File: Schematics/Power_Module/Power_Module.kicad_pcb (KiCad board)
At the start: 4 copper layers, 69.5 x 60 mm, 1 part, among them J6 Stack Male Edge Connector

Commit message: Added PCB template
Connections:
- net Vbuck1 renamed 3.3V_A
- net Vbuck1.1 renamed 5.0V_A
- net Vbuck2 renamed 3.3V_B
- net Vin + renamed BATT_A
- net Vin - renamed GND
- net Vin 2+ renamed BATT_B
- net Vin2 - renamed GND2
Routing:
- added copper zone on In1.Cu, net GND
- added copper zone on In2.Cu, net GND
- removed copper zone on In1.Cu, net (none)
- removed copper zone on In2.Cu, net (none)
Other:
- board text added: "PLACE POWER CONNECTORS HERE (okay if on bottom)"
- board text removed: "Make sure connectors are at the front (on both sides is fine)"

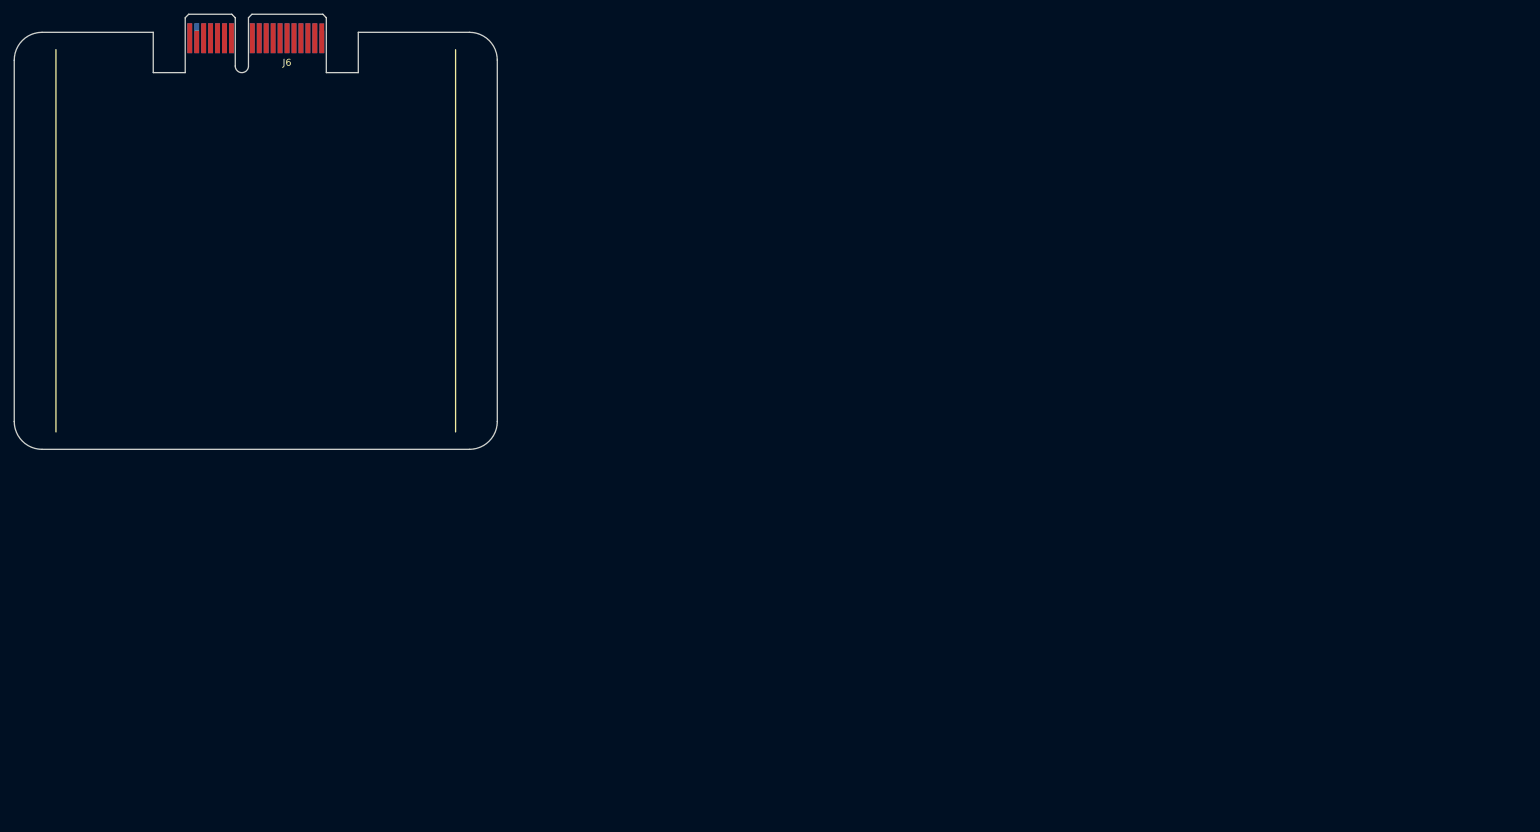
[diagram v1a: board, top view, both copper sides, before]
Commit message: Layout of 3.3V_A converter finished
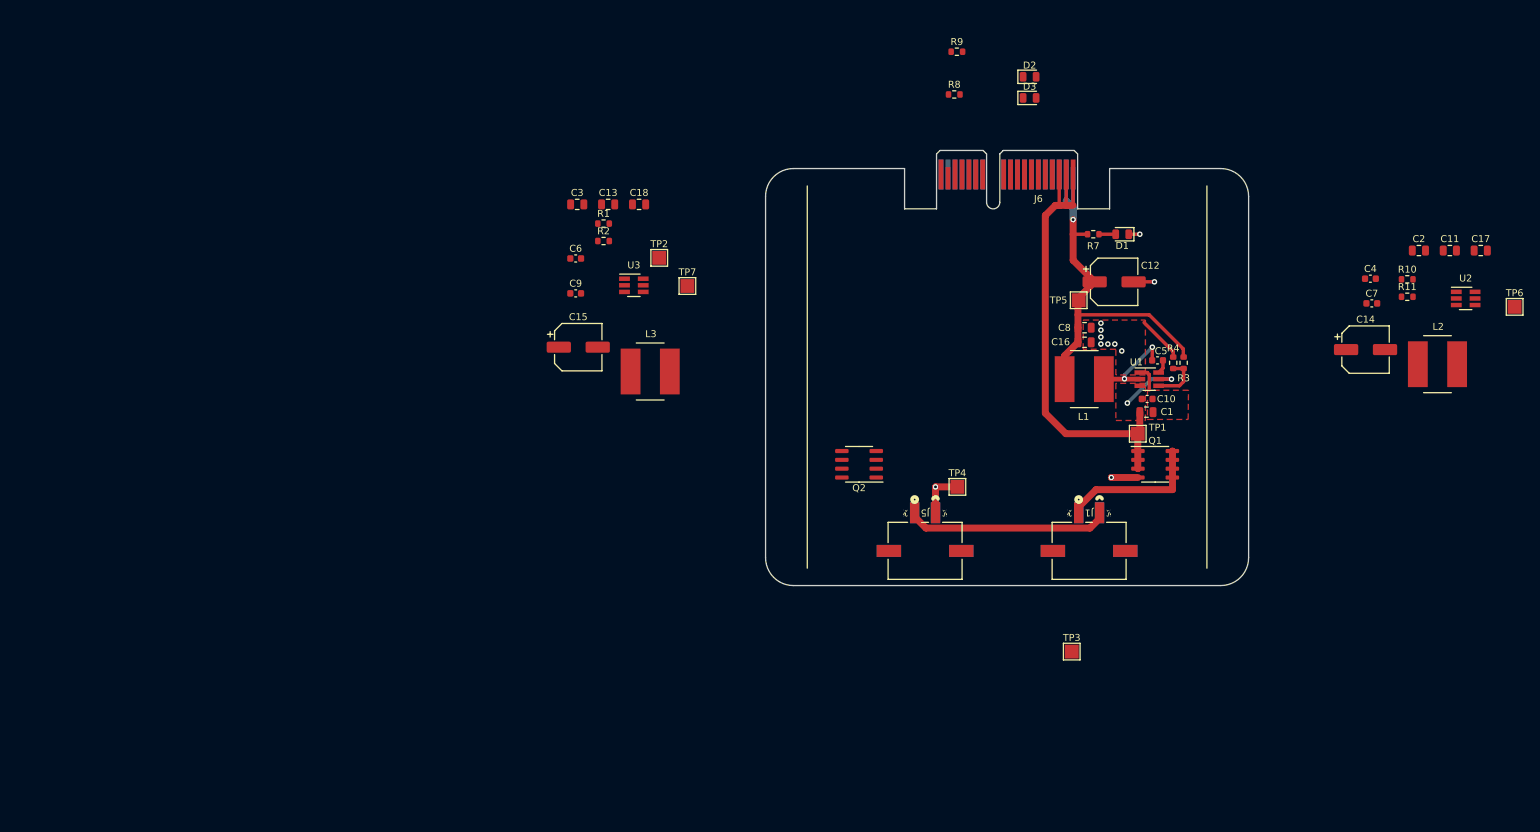
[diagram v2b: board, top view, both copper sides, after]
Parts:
- added C1: 4.7uF, Capacitor_SMD:C_0805_2012Metric, F.Cu at (185.1, 74.8)
- added C10: 100nF, Capacitor_SMD:C_0603_1608Metric, F.Cu at (185.2, 72.9)
- added C11: 22uF, Capacitor_SMD:C_0805_2012Metric, F.Cu at (228.7, 51.5)
- added C12: 100uF, Capacitor_SMD:CP_Elec_6.3x5.9, F.Cu at (180.4, 56.0)
- added C13: 22uF, Capacitor_SMD:C_0805_2012Metric, F.Cu at (107.6, 44.9)
- added C14: 100uF, Capacitor_SMD:CP_Elec_6.3x5.9, F.Cu at (216.6, 65.8)
- added C15: 100uF, Capacitor_SMD:CP_Elec_6.3x5.9, F.Cu at (103.3, 65.5)
- added C16: 22uF, Capacitor_SMD:C_0805_2012Metric, F.Cu at (176.2, 64.8)
- added C17: 22uF, Capacitor_SMD:C_0805_2012Metric, F.Cu at (233.2, 51.5)
- added C18: 22uF, Capacitor_SMD:C_0805_2012Metric, F.Cu at (112.0, 44.9)
- added C2: 4.7uF, Capacitor_SMD:C_0805_2012Metric, F.Cu at (224.2, 51.5)
- added C3: 4.7uF, Capacitor_SMD:C_0805_2012Metric, F.Cu at (103.2, 44.9)
- added C4: 100nF, Capacitor_SMD:C_0603_1608Metric, F.Cu at (217.3, 55.6)
- added C5: 100nF, Capacitor_SMD:C_0603_1608Metric, F.Cu at (186.7, 67.3)
- added C6: 100nF, Capacitor_SMD:C_0603_1608Metric, F.Cu at (102.9, 52.7)
- added C7: 100nF, Capacitor_SMD:C_0603_1608Metric, F.Cu at (217.5, 59.1)
- added C8: 22uF, Capacitor_SMD:C_0805_2012Metric, F.Cu at (176.2, 62.6)
- added C9: 100nF, Capacitor_SMD:C_0603_1608Metric, F.Cu at (102.9, 57.7)
- added D1: 3.3V_A PWR (GRN), LED_SMD:LED_0805_2012Metric, F.Cu at (181.6, 49.2)
- added D2: 5.0V_A PWR (RED), LED_SMD:LED_0805_2012Metric, F.Cu at (168.2, 26.6)
- added D3: 3.3V_B PWR (GRN), LED_SMD:LED_0805_2012Metric, F.Cu at (168.2, 29.6)
- added J1: ScrewSwitch A, footprints:CONN_2-1445057-2_TYCO, F.Cu at (178.3, 89.3)
- added J2: ScrewSwitch B, footprints:CONN_2-1445057-2_TYCO, B.Cu at (175.3, 89.3)
- added J3: Battery B, footprints:CONN_2-1445057-2_TYCO, B.Cu at (151.7, 89.3)
- added J5: Battery A, footprints:CONN_2-1445057-2_TYCO, F.Cu at (154.7, 89.3)
- added L1: 5.6uH, Inductor_SMD:L_Bourns_SRN8040TA, F.Cu at (176.1, 70.0)
- added L2: 6.8uH, Inductor_SMD:L_Bourns_SRN8040TA, F.Cu at (226.9, 67.9)
- added L3: 5.6uH, Inductor_SMD:L_Bourns_SRN8040TA, F.Cu at (113.7, 69.0)
- added Q1: AO4447A, Package_SO:SOIC-8_3.9x4.9mm_P1.27mm, F.Cu at (186.3, 82.3)
- added Q2: AO4447A, Package_SO:SOIC-8_3.9x4.9mm_P1.27mm, F.Cu at (143.7, 82.3)
- added R1: 100k, Resistor_SMD:R_0603_1608Metric, F.Cu at (106.9, 47.7)
- added R10: 56k, Resistor_SMD:R_0603_1608Metric, F.Cu at (222.6, 55.7)
- added R11: 7.5k, Resistor_SMD:R_0603_1608Metric, F.Cu at (222.6, 58.2)
- added R2: 22k, Resistor_SMD:R_0603_1608Metric, F.Cu at (106.9, 50.2)
- added R3: 100k, Resistor_SMD:R_0603_1608Metric, F.Cu at (190.4, 67.7)
- added R4: 22k, Resistor_SMD:R_0603_1608Metric, F.Cu at (188.9, 67.7)
- added R7: 510R, Resistor_SMD:R_0603_1608Metric, F.Cu at (177.4, 49.2)
- added R8: 2k, Resistor_SMD:R_0603_1608Metric, F.Cu at (157.4, 29.1)
- added R9: 510R, Resistor_SMD:R_0603_1608Metric, F.Cu at (157.8, 22.9)
- added TP1: TP_BATT1, TestPoint:TestPoint_Pad_2.0x2.0mm, F.Cu at (183.8, 77.9)
- added TP2: TP_BATT2, TestPoint:TestPoint_Pad_2.0x2.0mm, F.Cu at (115.0, 52.6)
- added TP3: TP_GND2, TestPoint:TestPoint_Pad_2.0x2.0mm, F.Cu at (174.3, 109.2)
- added TP4: TP_GND1, TestPoint:TestPoint_Pad_2.0x2.0mm, F.Cu at (157.8, 85.5)
- added TP5: TP_3.3V_A, TestPoint:TestPoint_Pad_2.0x2.0mm, F.Cu at (175.3, 58.7)
- added TP6: TP_5.0V_A, TestPoint:TestPoint_Pad_2.0x2.0mm, F.Cu at (238.0, 59.6)
- added TP7: TP_3.3V_B, TestPoint:TestPoint_Pad_2.0x2.0mm, F.Cu at (119.0, 56.6)
- added U1: LMR51430XDDCR, Package_TO_SOT_SMD:SOT-23-6_Handsoldering, F.Cu at (185.4, 70.0)
- added U2: LMR51430XDDCR, Package_TO_SOT_SMD:SOT-23-6_Handsoldering, F.Cu at (231.0, 58.4)
- added U3: LMR51430XDDCR, Package_TO_SOT_SMD:SOT-23-6_Handsoldering, F.Cu at (111.3, 56.5)
- moved J6 109.9 mm to (174.5, 40.6)
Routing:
- net BATT_A: track 0.00 -> 78.9 mm, vias 0 -> 2
- net 3.3V_A: track 0.00 -> 57.6 mm, vias 0 -> 1
- net Net-(J1-Pad1): track 0.00 -> 29.2 mm
- net GND: track 0.00 -> 25.7 mm, vias 0 -> 11
- net Net-(J1-Pad2): track 0.00 -> 20.9 mm
- net Net-(U1-SW): track 0.00 -> 13.3 mm, vias 0 -> 2
- net Net-(U1-FB): track 0.00 -> 7.22 mm
- net Net-(D1-A): track 0.00 -> 2.40 mm
- net Net-(U1-CB): track 0.00 -> 2.01 mm
- added copper zone on F.Cu, net BATT_A
- added copper zone on F.Cu, net GND

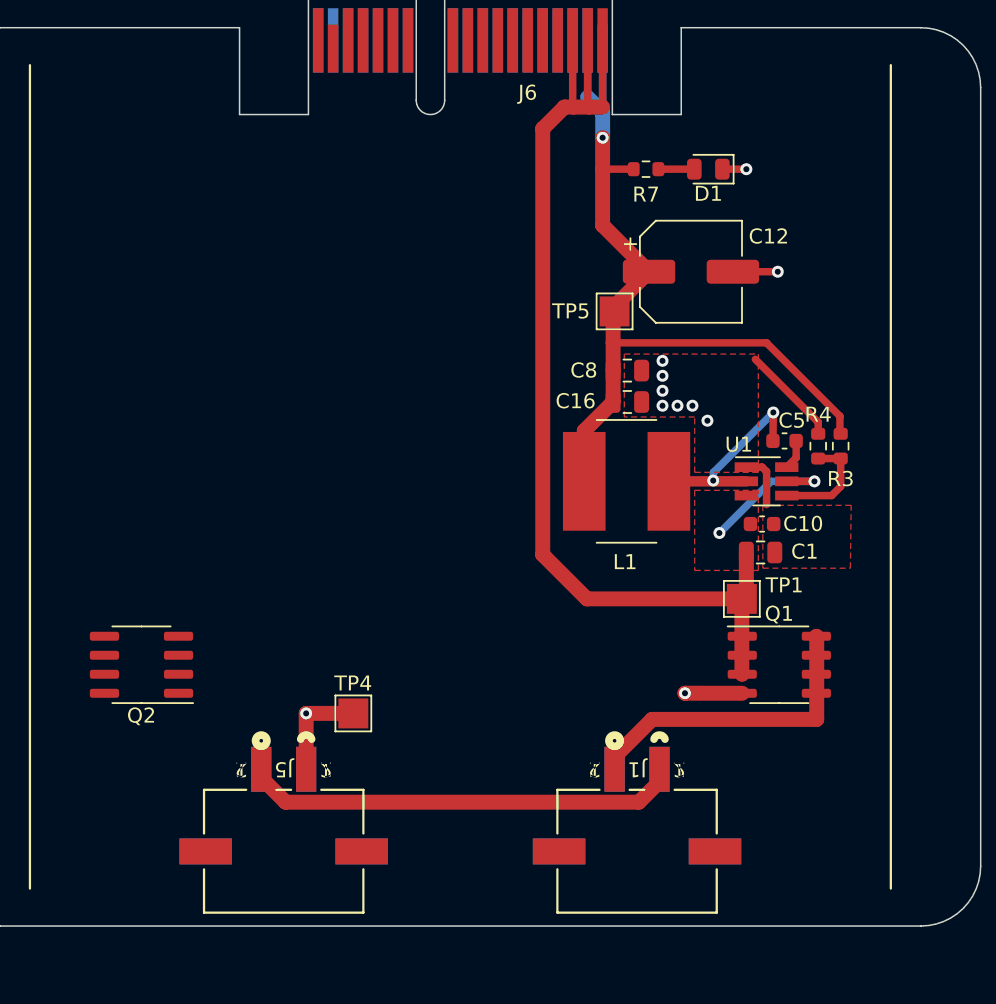
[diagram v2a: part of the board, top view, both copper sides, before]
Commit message: Tweaked arrangement and updated copper clearance
-Set "copper to edge clearance" to 0.3mm
-Moved molex connectors 8mm back from board edge
-Decreased horizontal margin from 2.5mm to 1.25mm
-Increased several traces from 1mm to 2mm
-Added a few more copper pours
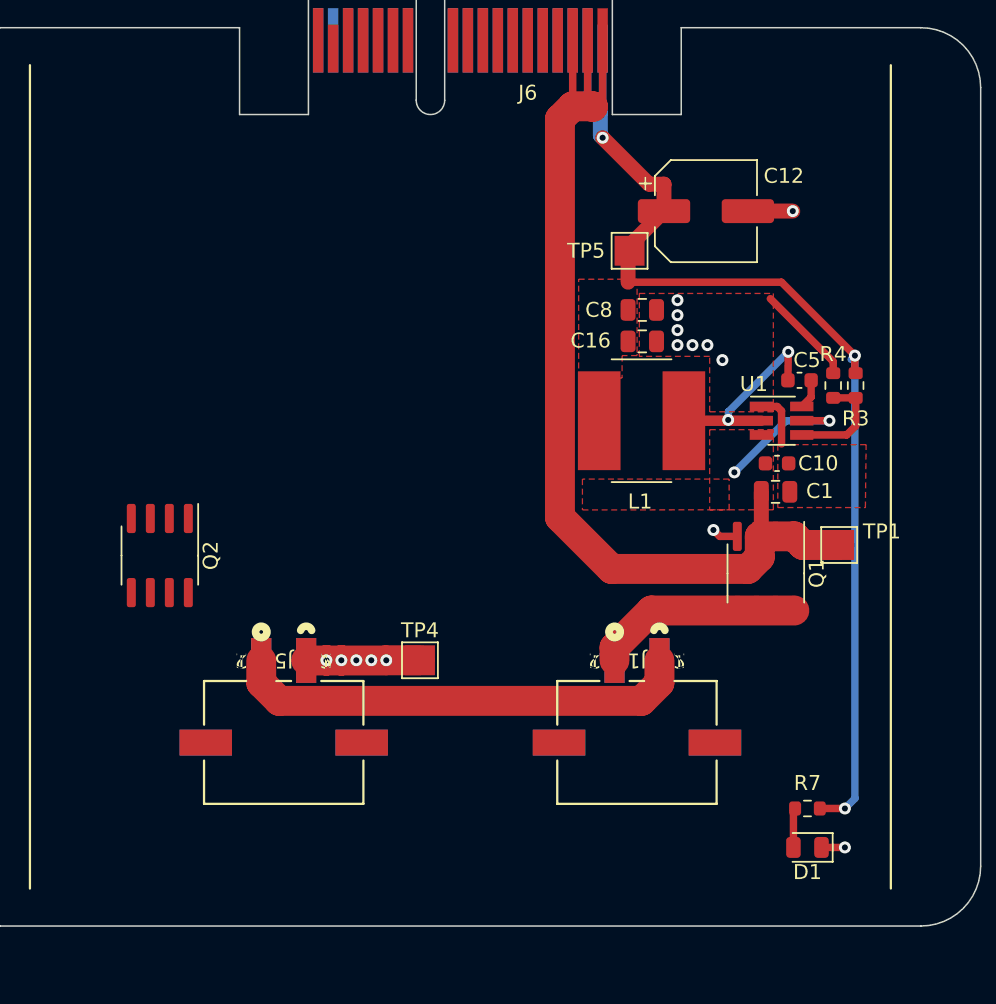
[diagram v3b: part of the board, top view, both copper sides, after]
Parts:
- moved D1 45.8 mm to (188.2, 94.5)
- moved R7 44.0 mm to (188.2, 91.9), turned to 180 degrees
- moved TP1 7.43 mm to (190.3, 74.3)
- moved Q2 7.40 mm to (144.9, 75.0), turned to -90 degrees
- moved J1 7.27 mm to (178.3, 82.0)
- moved J2 7.27 mm to (175.3, 82.0)
- moved J3 7.27 mm to (151.7, 82.0)
- moved J5 7.27 mm to (154.7, 82.0)
- moved Q1 6.17 mm to (185.4, 76.2), turned to -90 degrees
- moved TP4 5.69 mm to (162.3, 82.0)
- moved C10 4.17 mm to (186.2, 68.8)
- moved R3 4.17 mm to (191.4, 63.6)
- moved R4 4.17 mm to (189.9, 63.6)
- moved TP5 4.17 mm to (176.3, 54.6)
- moved C1 4.17 mm to (186.1, 70.8)
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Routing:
- net 3.3V_A: track 57.6 -> 75.0 mm, vias 1 -> 3
- net Net-(J1-Pad2): track 20.9 -> 13.9 mm
- net BATT_A: track 78.9 -> 77.1 mm
- net GND: track 25.7 -> 24.3 mm, vias 11 -> 15
- net Net-(J1-Pad1): track 29.2 -> 30.6 mm
- added copper zone on F.Cu, net 3.3V_A

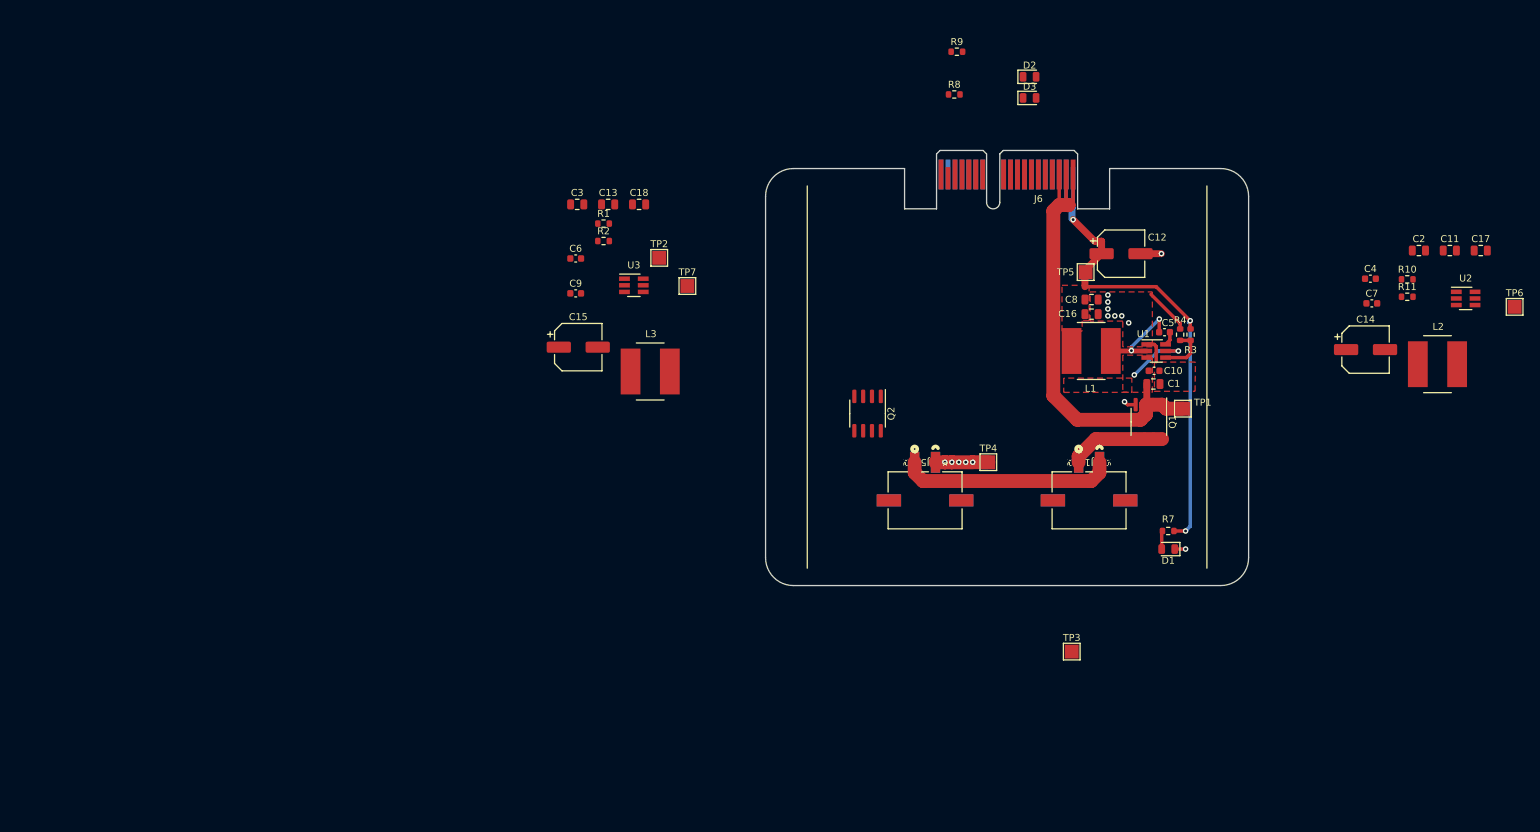
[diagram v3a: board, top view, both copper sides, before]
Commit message: First draft of layout finished, all DRC passed
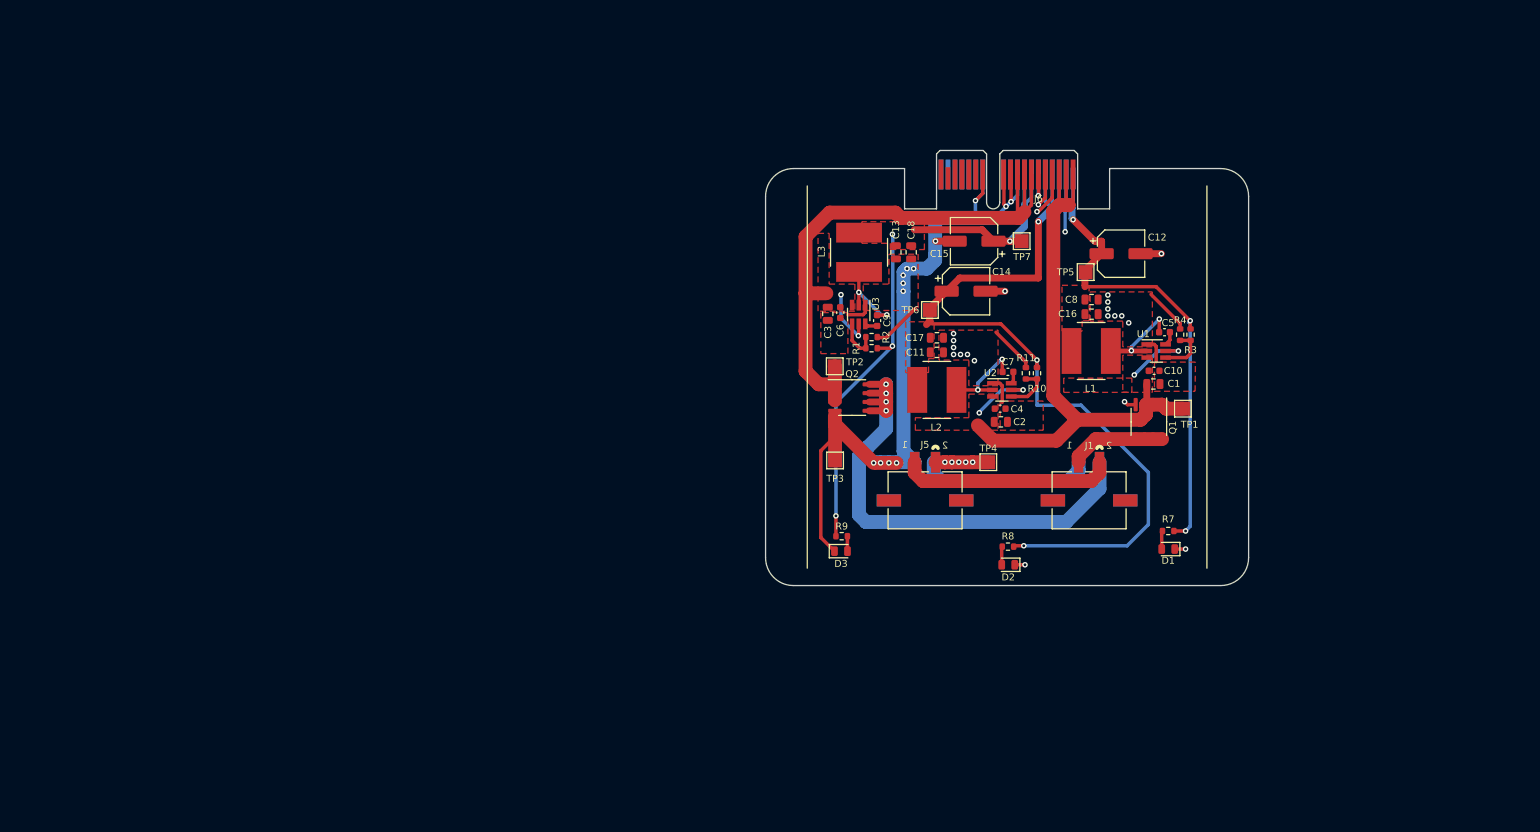
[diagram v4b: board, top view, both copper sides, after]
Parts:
- moved TP6 84.1 mm to (153.9, 60.1)
- moved C17 79.3 mm to (154.9, 64.1)
- moved C11 75.2 mm to (154.9, 66.2)
- moved L2 72.1 mm to (154.9, 71.6), turned to 180 degrees
- moved R9 71.7 mm to (141.2, 92.7)
- moved D3 70.6 mm to (141.1, 94.8)
- moved D2 70.3 mm to (165.2, 96.8), turned to 180 degrees
- moved U2 68.0 mm to (164.2, 71.6)
- moved R8 65.5 mm to (165.1, 94.2), turned to 180 degrees
- moved C2 65.0 mm to (164.1, 76.2)
- moved C15 59.0 mm to (160.2, 50.2), turned to 180 degrees
- moved C14 58.1 mm to (159.1, 57.4)
- moved C4 56.5 mm to (164.0, 74.3)
- moved R11 56.0 mm to (167.7, 69.2), turned to 90 degrees
- moved R10 55.0 mm to (169.3, 69.2), turned to -90 degrees
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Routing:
- net GND2: track 0.00 -> 127.8 mm, vias 0 -> 13
- net 5.0V_A: track 0.00 -> 114.1 mm, vias 0 -> 3
- net BATT_B: track 0.00 -> 92.2 mm, vias 0 -> 2
- net 3.3V_B: track 0.00 -> 80.1 mm, vias 0 -> 4
- net Net-(J2-Pad2): track 0.00 -> 74.9 mm, vias 0 -> 4
- net GND: track 24.3 -> 65.5 mm, vias 15 -> 28
- net BATT_A: track 77.1 -> 103.2 mm, vias 2 -> 4
- net Net-(J2-Pad1): track 0.00 -> 24.7 mm
- net Net-(U2-SW): track 0.00 -> 13.0 mm, vias 0 -> 2
- net Net-(U3-SW): track 0.00 -> 11.5 mm, vias 0 -> 2
- net Net-(U2-FB): track 0.00 -> 7.03 mm
- net Net-(U3-FB): track 0.00 -> 6.43 mm
- net Net-(D2-A): track 0.00 -> 2.75 mm
- net Net-(D3-A): track 0.00 -> 2.16 mm
- net Net-(U3-CB): track 0.00 -> 1.82 mm
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- added copper zone on F.Cu, net 3.3V_B
- added copper zone on F.Cu, net 5.0V_A
- added copper zone on F.Cu, net BATT_B
- added copper zone on F.Cu, net GND2
